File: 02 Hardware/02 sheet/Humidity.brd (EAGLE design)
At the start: 86 x 64 mm, 24 parts, among them IC1 IRM-03, IC2 ESP8266, J1 AC 230V, J2 Fan, J3 DHT22_OUT, J4 DHT22_IN, K1 351, Q1 TRANSISTOR-NPN_BC817SMD

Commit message: Signed-off-by: Joe G <grabow@amesys.de>
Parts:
- J3: value DHT22_OUT -> AM2302_OUT
- J4: value DHT22_IN -> AM2302_IN
- Q1: value TRANSISTOR-NPN_BC817SMD -> BC817
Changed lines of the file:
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@@
 </autorouter>
 <elements>
-<element name="J4" library="Eagle_WR-TBL Rising Cage Clamp (rev20a)" package="691216710003" package3d_urn="urn:adsk.eagle:package:16248490/2" value="DHT22_IN" x="5" y="9.5" smashed="yes" rot="R270">
+<element name="J4" library="Eagle_WR-TBL Rising Cage Clamp (rev20a)" package="691216710003" package3d_urn="urn:adsk.eagle:package:16248490/2" value="AM2302_IN" x="5" y="9.5" smashed="yes" rot="R270">
 <attribute name="DATASHEET-URL" value="https://www.we-online.com/catalog/datasheet/691216710003.pdf" x="5" y="9.5" size="1.778" layer="27" rot="R270" display="off"/>
 <attribute name="IR-UL" value="14A" x="5" y="9.5" size="1.778" layer="27" rot="R270" display="off"/>
@@
 <attribute name="WORKING-VOLTAGE-VDE" value="250V (AC)" x="5" y="9.5" size="1.778" layer="27" rot="R270" display="off"/>
 </element>
-<element name="J3" library="Eagle_WR-TBL Rising Cage Clamp (rev20a)" package="691216710003" package3d_urn="urn:adsk.eagle:package:16248490/2" value="DHT22_OUT" x="5" y="29.8" smashed="yes" rot="R270">
+<element name="J3" library="Eagle_WR-TBL Rising Cage Clamp (rev20a)" package="691216710003" package3d_urn="urn:adsk.eagle:package:16248490/2" value="AM2302_OUT" x="5" y="29.8" smashed="yes" rot="R270">
 <attribute name="DATASHEET-URL" value="https://www.we-online.com/catalog/datasheet/691216710003.pdf" x="5" y="29.8" size="1.778" layer="27" rot="R270" display="off"/>
 <attribute name="IR-UL" value="14A" x="5" y="29.8" size="1.778" layer="27" rot="R270" display="off"/>
@@
 <attribute name="VALUE" x="25.3274" y="51.2744" size="0.9906" layer="28" ratio="10" rot="MR90"/>
 </element>
-<element name="Q1" library="Aeternum" package="TRANSISTOR-NPN_SOT23-BEC" value="TRANSISTOR-NPN_BC817SMD" x="40.41" y="59.08" smashed="yes" rot="MR90">
+<element name="Q1" library="Aeternum" package="TRANSISTOR-NPN_SOT23-BEC" value="BC817" x="40.41" y="59.08" smashed="yes" rot="MR90">
 <attribute name="NAME" x="37.315" y="54.675" size="1.27" layer="26" rot="MR90"/>
 <attribute name="VALUE" x="37.235" y="57.175" size="1.27" layer="28" rot="MR90"/>

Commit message: with AMICA Package
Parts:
- IC2: value ESP8266 -> Amica Modul V2 ESP8266 ESP-12F
- R1: value 120 -> 180
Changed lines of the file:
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@@
 <attribute name="VALUE" x="49.52" y="53.231" size="1.778" layer="27" ratio="10"/>
 </element>
-<element name="R1" library="rcl" library_urn="urn:adsk.eagle:library:334" package="R1206" package3d_urn="urn:adsk.eagle:package:23540/2" value="120" x="36.578" y="32.11" smashed="yes" rot="MR0">
+<element name="R1" library="rcl" library_urn="urn:adsk.eagle:library:334" package="R1206" package3d_urn="urn:adsk.eagle:package:23540/2" value="180" x="36.578" y="32.11" smashed="yes" rot="MR0">
 <attribute name="NAME" x="33.118" y="31.4054" size="1.27" layer="26" ratio="10" rot="MR0"/>
 <attribute name="POPULARITY" value="41" x="36.578" y="32.11" size="1.778" layer="28" rot="MR0" display="off"/>
@@
 <attribute name="VALUE" x="37.587" y="47.297" size="1.27" layer="28" ratio="10" rot="MR180"/>
 </element>
-<element name="IC2" library="ESP12E_DEVKIT" package="ESP12E_DEVKIT" value="ESP8266" x="31.5" y="32" smashed="yes">
+<element name="IC2" library="ESP12E_DEVKIT" package="ESP12E_DEVKIT" value="Amica Modul V2 ESP8266 ESP-12F" x="31.5" y="32" smashed="yes">
 <attribute name="NAME" x="33.05" y="35.46" size="1.27" layer="25" rot="R180"/>
 <attribute name="VALUE" x="27.45" y="5.69" size="1.27" layer="27"/>

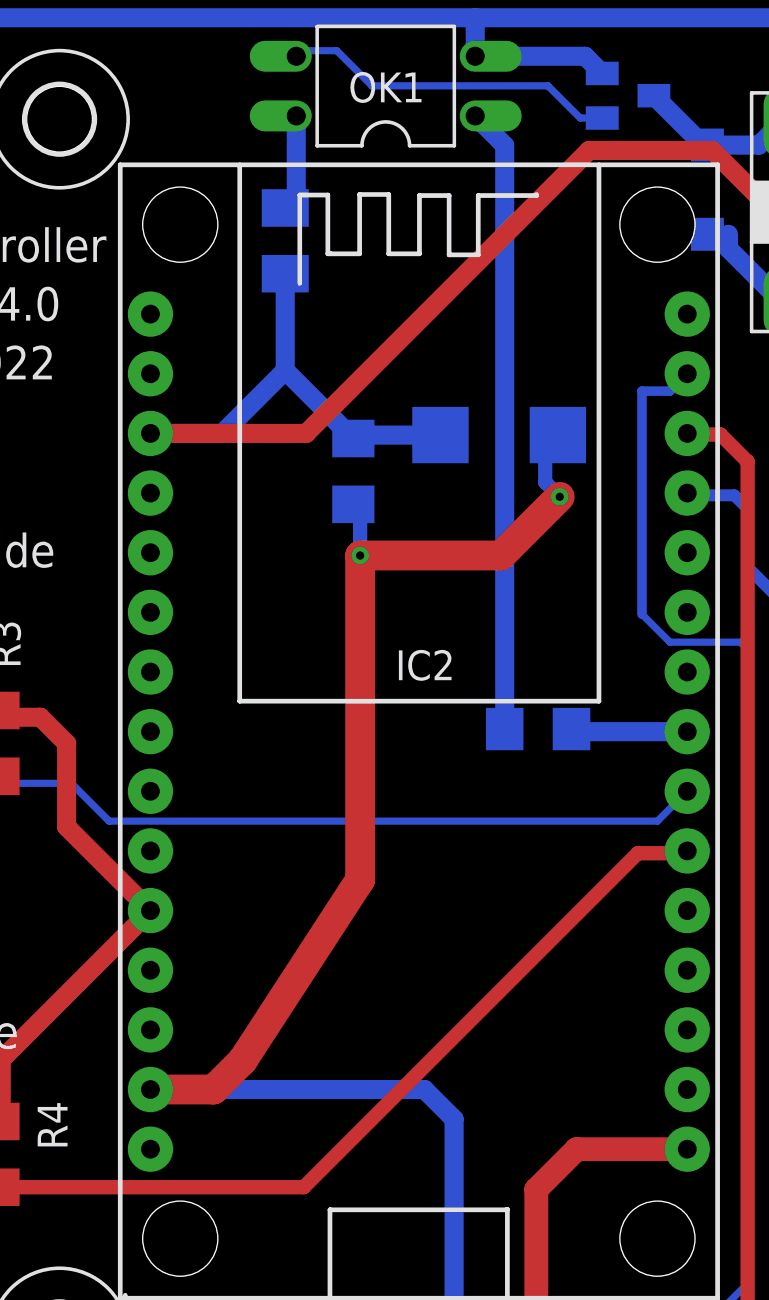
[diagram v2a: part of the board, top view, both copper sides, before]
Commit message: Dugfix Boarddesign
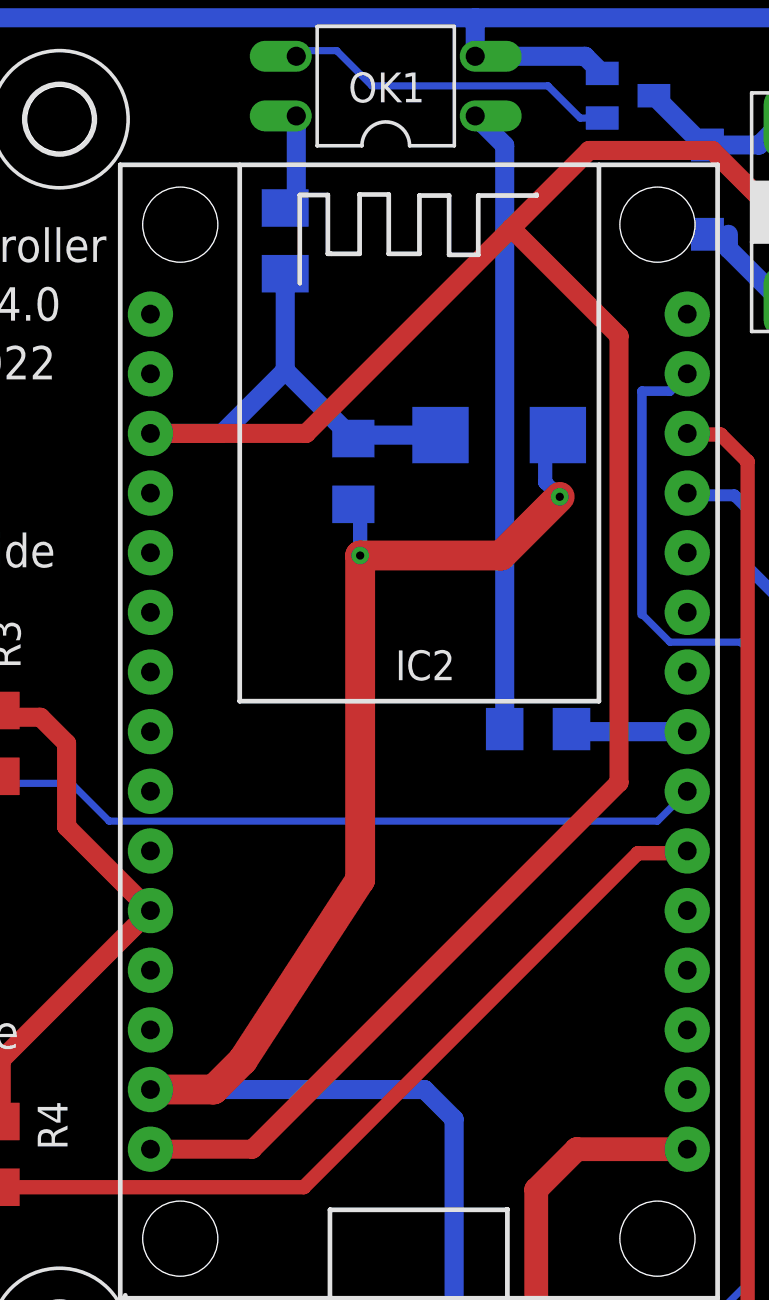
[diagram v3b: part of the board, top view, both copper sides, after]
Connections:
- net +5V: now also IC2.VIN
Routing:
- net +5V: track 102.8 -> 154.7 mm
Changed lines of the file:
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@@
 <layer number="17" name="Pads" color="2" fill="1" visible="yes" active="yes"/>
 <layer number="18" name="Vias" color="2" fill="1" visible="yes" active="yes"/>
-<layer number="19" name="Unrouted" color="6" fill="1" visible="no" active="yes"/>
+<layer number="19" name="Unrouted" color="6" fill="1" visible="yes" active="yes"/>
 <layer number="20" name="Dimension" color="24" fill="1" visible="yes" active="yes"/>
 <layer number="21" name="tPlace" color="7" fill="1" visible="yes" active="yes"/>
@@
 <wire x1="44.6824" y1="53.18" x2="44.6824" y2="52.5676" width="0.8128" layer="16"/>
 <wire x1="26.7" y1="44.7" x2="20.07" y2="44.7" width="0.8128" layer="1"/>
-<wire x1="38.75" y1="56.75" x2="26.7" y2="44.7" width="0.8128" layer="1"/>
+<wire x1="38.75" y1="56.75" x2="35.43700625" y2="53.43700625" width="0.8128" layer="1"/>
+<wire x1="35.43700625" y1="53.43700625" x2="26.7" y2="44.7" width="0.8128" layer="1"/>
 <wire x1="20.07" y1="44.7" x2="23.13" y2="44.7" width="0.8128" layer="16"/>
 <wire x1="23.13" y1="44.7" x2="25.81" y2="47.38" width="0.8128" layer="16"/>
@@
 <wire x1="50.58" y1="37.75" x2="50.58" y2="10.342" width="1.016" layer="1"/>
 <wire x1="50.58" y1="10.342" x2="50.5" y2="10.262" width="1.016" layer="1"/>
+<contactref element="IC2" pad="VIN"/>
+<wire x1="20.07" y1="14.22" x2="24.410984375" y2="14.22" width="0.8128" layer="1"/>
+<wire x1="24.410984375" y1="14.22" x2="40.023084375" y2="29.8321" width="0.8128" layer="1"/>
+<wire x1="40.023084375" y1="29.8321" x2="40.023084375" y2="48.850928125" width="0.8128" layer="1"/>
+<wire x1="40.023084375" y1="48.850928125" x2="35.43700625" y2="53.43700625" width="0.8128" layer="1"/>
 </signal>
 <signal name="N$8">

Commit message: Schaltung
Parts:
- moved D1 1.19 mm to (45.0, 55.1), turned to 90 degrees
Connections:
- net +5V: now also D1.C; no longer D1.A
- net N$8: now also D1.A; no longer D1.C
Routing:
- net +5V: track 154.7 -> 153.8 mm
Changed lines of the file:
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@@
 <layers>
 <layer number="1" name="Top" color="4" fill="1" visible="yes" active="yes"/>
-<layer number="16" name="Bottom" color="1" fill="1" visible="no" active="yes"/>
+<layer number="16" name="Bottom" color="1" fill="1" visible="yes" active="yes"/>
 <layer number="17" name="Pads" color="2" fill="1" visible="yes" active="yes"/>
 <layer number="18" name="Vias" color="2" fill="1" visible="yes" active="yes"/>
 <layer number="19" name="Unrouted" color="6" fill="1" visible="yes" active="yes"/>
 <layer number="20" name="Dimension" color="24" fill="1" visible="yes" active="yes"/>
-<layer number="21" name="tPlace" color="7" fill="1" visible="yes" active="yes"/>
-<layer number="22" name="bPlace" color="7" fill="1" visible="no" active="yes"/>
+<layer number="21" name="tPlace" color="7" fill="1" visible="no" active="yes"/>
+<layer number="22" name="bPlace" color="7" fill="1" visible="yes" active="yes"/>
 <layer number="23" name="tOrigins" color="15" fill="1" visible="no" active="yes"/>
-<layer number="24" name="bOrigins" color="15" fill="1" visible="no" active="yes"/>
+<layer number="24" name="bOrigins" color="15" fill="1" visible="yes" active="yes"/>
 <layer number="25" name="tNames" color="7" fill="1" visible="yes" active="yes"/>
-<layer number="26" name="bNames" color="7" fill="1" visible="no" active="yes"/>
+<layer number="26" name="bNames" color="7" fill="1" visible="yes" active="yes"/>
 <layer number="27" name="tValues" color="7" fill="1" visible="no" active="yes"/>
 <layer number="28" name="bValues" color="7" fill="1" visible="no" active="yes"/>
@@
 <attribute name="VALUE" x="37.235" y="57.175" size="1.27" layer="28" rot="MR90"/>
 </element>
-<element name="D1" library="diode" library_urn="urn:adsk.eagle:library:210" package="SOD123" package3d_urn="urn:adsk.eagle:package:43420/1" value="1N4148" x="43.79" y="55.08" smashed="yes" rot="MR270">
-<attribute name="NAME" x="46.29" y="56.18" size="1.27" layer="26" rot="MR270"/>
-<attribute name="POPULARITY" value="22" x="43.79" y="55.08" size="1.778" layer="28" rot="MR270" display="off"/>
-<attribute name="VALUE" x="46.09" y="56.18" size="1.27" layer="28" rot="MR270"/>
+<element name="D1" library="diode" library_urn="urn:adsk.eagle:library:210" package="SOD123" package3d_urn="urn:adsk.eagle:package:43420/1" value="1N4148" x="44.981996875" y="55.10393125" smashed="yes" rot="MR90">
+<attribute name="NAME" x="42.6724125" y="54.49905625" size="1.27" layer="26" rot="MR90"/>
+<attribute name="POPULARITY" value="22" x="44.981996875" y="55.10393125" size="1.778" layer="28" rot="MR90" display="off"/>
+<attribute name="VALUE" x="42.681996875" y="54.00393125" size="1.27" layer="28" rot="MR90"/>
 </element>
 <element name="C1" library="rcl" library_urn="urn:adsk.eagle:library:334" package="C1206" package3d_urn="urn:adsk.eagle:package:23618/2" value="100n" x="28.71" y="43.08" smashed="yes" rot="MR270">
@@
 <contactref element="R2" pad="1"/>
 <contactref element="K1" pad="1"/>
-<contactref element="D1" pad="A"/>
 <contactref element="C1" pad="1"/>
 <contactref element="IC1" pad="+"/>
@@
 <wire x1="28.71" y1="44.48" x2="28.86" y2="44.63" width="0.8128" layer="16"/>
 <wire x1="28.86" y1="44.63" x2="32.42" y2="44.63" width="0.8128" layer="16"/>
-<wire x1="43.79" y1="53.18" x2="44.6824" y2="53.18" width="0.3048" layer="16"/>
 <wire x1="44" y1="56.75" x2="38.75" y2="56.75" width="0.8128" layer="1"/>
 <wire x1="46.94" y1="50.31" x2="46.94" y2="53.81" width="0.8128" layer="1"/>
@@
 <wire x1="40.023084375" y1="29.8321" x2="40.023084375" y2="48.850928125" width="0.8128" layer="1"/>
 <wire x1="40.023084375" y1="48.850928125" x2="35.43700625" y2="53.43700625" width="0.8128" layer="1"/>
+<contactref element="D1" pad="C"/>
+<wire x1="44.6824" y1="53.18" x2="44.981996875" y2="53.20393125" width="0" layer="19" extent="16-16"/>
 </signal>
 <signal name="N$8">
 <contactref element="K1" pad="16"/>
 <contactref element="Q1" pad="C"/>
-<contactref element="D1" pad="C"/>
 <wire x1="41.51" y1="59.08" x2="43.61" y2="56.98" width="0.8128" layer="16"/>
-<wire x1="43.61" y1="56.98" x2="43.79" y2="56.98" width="0.8128" layer="16"/>
-<wire x1="43.79" y1="56.98" x2="45.99" y2="56.98" width="0.8128" layer="16"/>
-<wire x1="45.99" y1="56.98" x2="46.94" y2="57.93" width="0.8128" layer="16"/>
+<wire x1="46.94" y1="57.93" x2="45.99" y2="56.98" width="0.8128" layer="16"/>
+<contactref element="D1" pad="A"/>
+<wire x1="43.61" y1="56.98" x2="44.958065625" y2="56.98" width="0.8128" layer="16"/>
+<wire x1="44.958065625" y1="56.98" x2="44.981996875" y2="57.00393125" width="0.1524" layer="16"/>
+<wire x1="45.99" y1="56.98" x2="45.005928125" y2="56.98" width="0.8128" layer="16"/>
+<wire x1="45.005928125" y1="56.98" x2="44.981996875" y2="57.00393125" width="0.1524" layer="16"/>
 </signal>
 <signal name="N$9">
